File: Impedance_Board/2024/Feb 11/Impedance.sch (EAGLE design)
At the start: 42 parts, among them U2 INA826AID, U4 MC74VHC1GT66DTT1, U7 AD8606ARZ, U8 AD8606ARZ

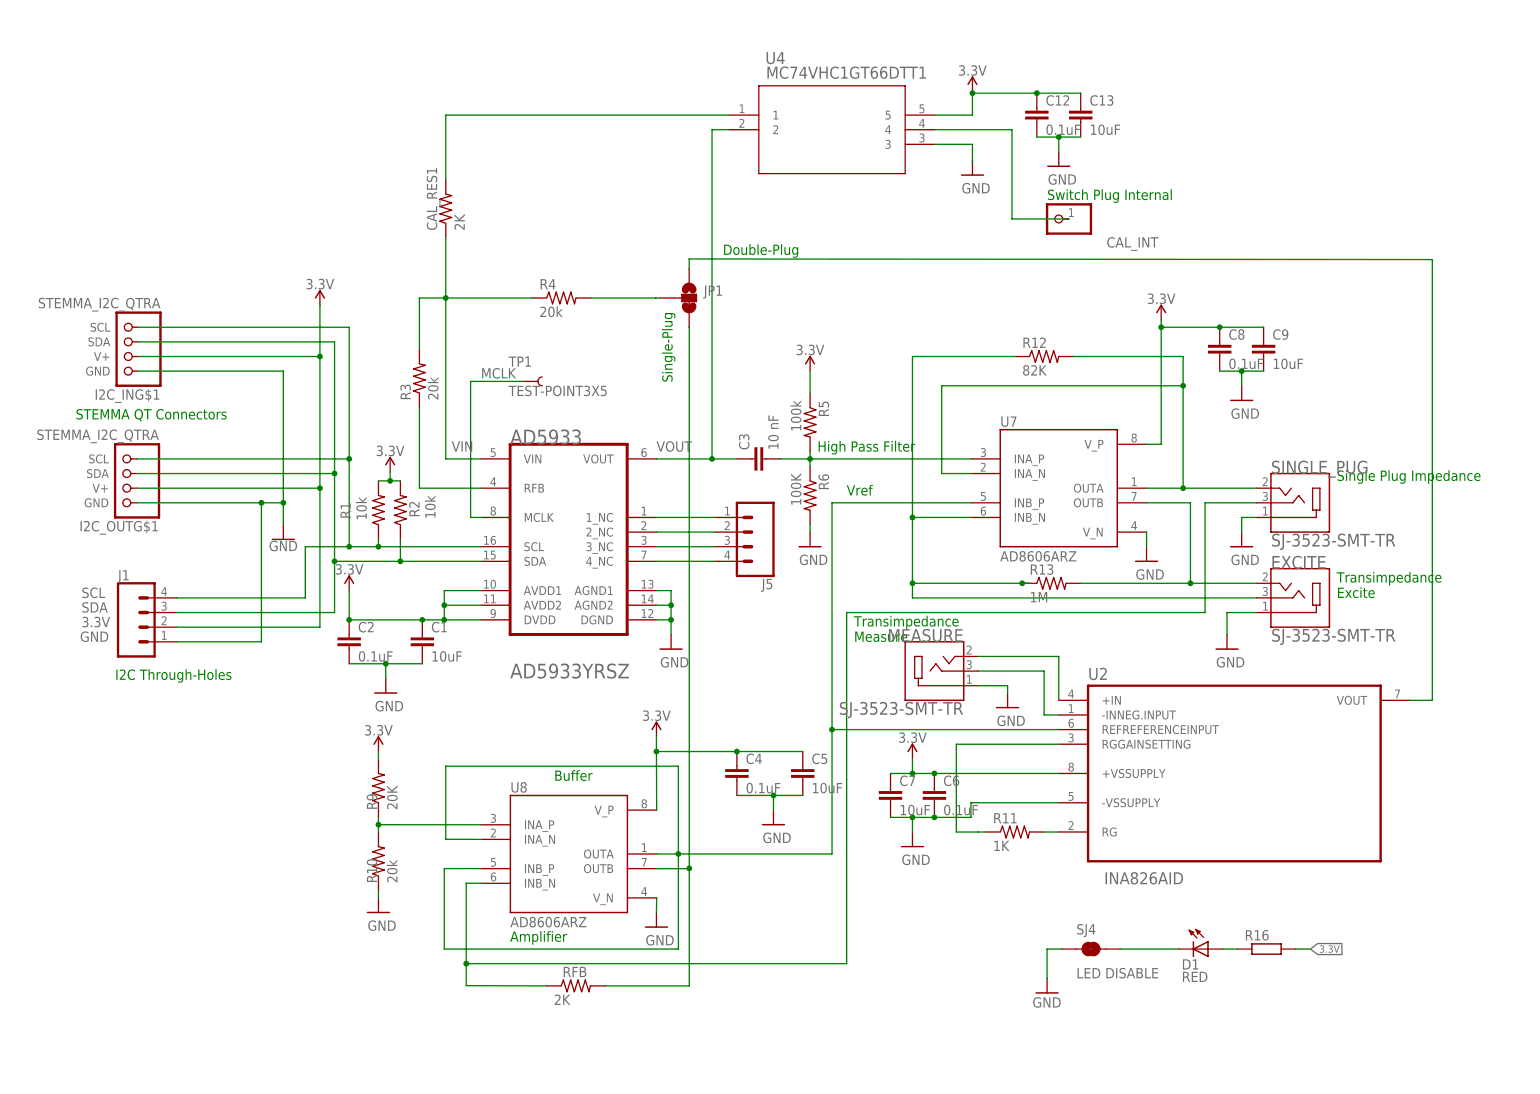
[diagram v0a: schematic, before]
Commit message: Impedance
Minor change SPO2
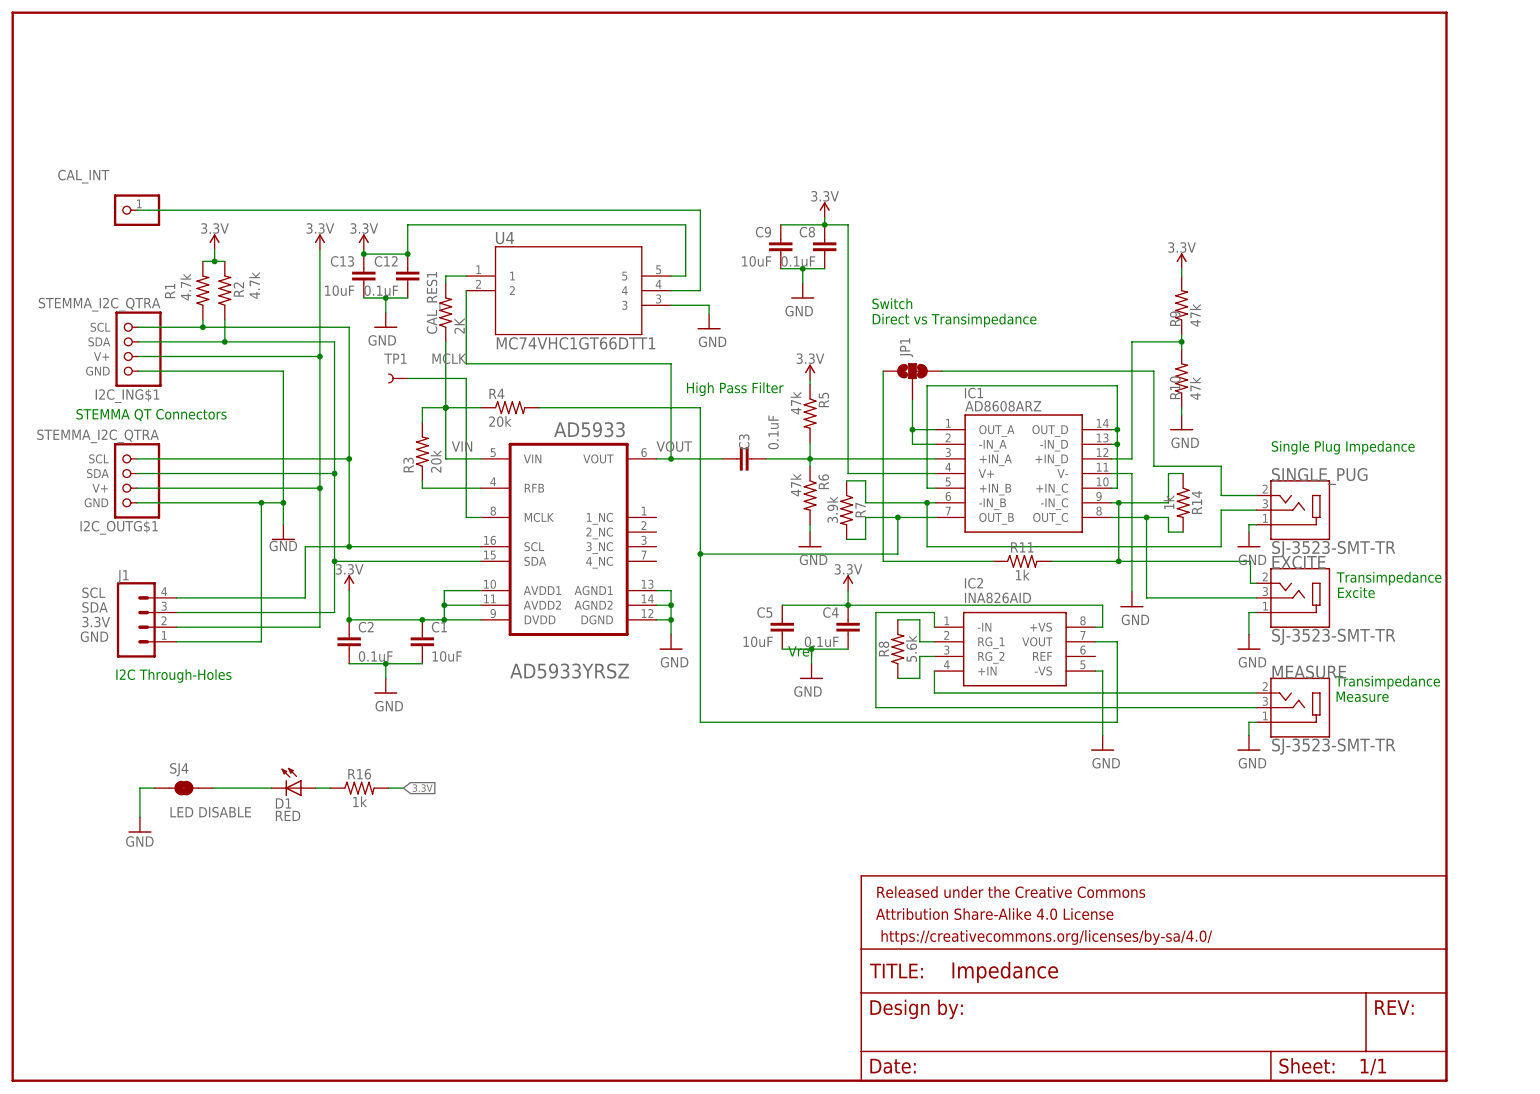
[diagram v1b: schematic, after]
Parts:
- removed C6: 0.1uF, rcl:C-EUC0603
- removed C7: 10uF, rcl:C-EUC0603
- removed J5: (no value), SparkFun-Connectors:CONN_04
- removed R12: 82K, rcl:R-US_R0603
- removed R13: 1M, rcl:R-US_R0603
- removed RFB: 2K, rcl:R-US_R0603
- removed U2: INA826AID, INA826AID:INA826AID
- removed U7, U8: AD8606ARZ, AD8606ARZ:AD8606ARZ
- added FRAME1: FRAME-LETTERNO_PACKAGE, SparkFun-Aesthetics:FRAME-LETTERNO_PACKAGE
- added IC1: AD8608ARZ, AD8608ARZ:AD8608ARZ
- added IC2: INA826AID, INA826AID:INA826AID
- added R14: 1k, SparkFun-Resistors:1KOHM-0603-1/10W-1%
- added R7: 3.9k, SparkFun-Resistors:3.9KOHM-0603-1/10W-1%
- added R8: 5.6k, SparkFun-Resistors:5.6KOHM-0603-1/10W-1%
- C3: value 10 nF -> 0.1uF; device rcl:C-EUC0603 -> SparkFun-Capacitors:0.1UF-0603-25V-(+80/-20%)
- R1, R2: value 10k -> 4.7k; device rcl:R-US_R0603 -> SparkFun-Resistors:4.7KOHM-0603-1/10W-1%
- R10: value 20k -> 47k; device rcl:R-US_R0603 -> SparkFun-Resistors:47KOHM-0603-1/10W-1%
- R11: value 1K -> 1k; device rcl:R-US_R0603 -> SparkFun-Resistors:1KOHM-0603-1/10W-1%
- R16: value R__0603 -> 1k; device JLC PCB Basic Parts_loc:R_1K_0603 -> SparkFun-Resistors:1KOHM-0603-1/10W-1%
- R3, R4: device rcl:R-US_R0603 -> SparkFun-Resistors:20KOHM-0603-1/10W-1%
- R5: value 100k -> 47k; device rcl:R-US_R0603 -> SparkFun-Resistors:47KOHM-0603-1/10W-1%
- R6: value 100K -> 47k; device rcl:R-US_R0603 -> SparkFun-Resistors:47KOHM-0603-1/10W-1%
- R9: value 20K -> 47k; device rcl:R-US_R0603 -> SparkFun-Resistors:47KOHM-0603-1/10W-1%
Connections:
- removed net N$10: AD5933.3_NC, J5.3
- removed net N$11: AD5933.4_NC, J5.4
- removed net N$16: R11.1, U2.RGGAINSETTING
- removed net N$17: RFB.1, SINGLE_PUG.3, U8.INB_N
- removed net N$3: AD5933.1_NC, J5.1
- removed net N$4: AD5933.2_NC, J5.2
- removed net N$7: RFB.2, U8.OUTB
- new net N$22: IC2.RG_1, R8.2
- new net N$6: C3.2, IC1.+IN_A, R5.2, R6.1
- net 3.3V: now also IC1.V+, IC2.+VS; no longer C6.1, C7.1, U2.+VSSUPPLY, U7.V_P, U8.V_P
- net GND: now also IC1.V-, IC2.-VS; no longer C6.2, C7.2, U2.-VSSUPPLY, U7.V_N, U8.V_N
- net N$1: now also IC1.-IN_B, R7.1, SINGLE_PUG.3; no longer JP1.2, R4.2
- net N$13: now also IC1.OUT_B, IC2.VOUT, R4.2, R7.2; no longer U2.REFREFERENCEINPUT, U7.INB_P, U8.INA_N, U8.INB_P, U8.OUTA
- net N$14: now also IC1.+IN_D; no longer U8.INA_P
- net N$15: now also JP1.3; no longer R12.2, U7.INA_N, U7.OUTA
- net N$18: now also IC1.+IN_B, IC1.+IN_C, IC1.-IN_D, IC1.OUT_D; no longer R11.2, U2.RG
- net N$19: now also IC1.-IN_C, R11.2, R14.1; no longer R13.2, U7.OUTB
- net N$20: now also IC2.+IN; no longer U2.+IN
- net N$21: now also IC2.-IN; no longer U2.-INNEG.INPUT
- net N$23: now also IC2.RG_2, R8.1; no longer EXCITE.3, R12.1, R13.1, U7.INB_N
- net N$25: now also EXCITE.3, IC1.OUT_C, R14.2; no longer JP1.1, U2.VOUT
- net N$8: now also JP1.1, R11.1; no longer JP1.3
- net N$9: now also IC1.-IN_A, IC1.OUT_A, JP1.2; no longer C3.2, R5.2, R6.1, U7.INA_P
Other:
- note added: "Switch Direct vs Transimpedance"
- note removed: "Amplifier"
- note removed: "Buffer"
- note removed: "Double-Plug"
- note removed: "Single-Plug"
- note removed: "Switch Plug Internal"
- moved on the sheet: C12, C13, C3, C4, C5, C8, C9, CAL_INT, CAL_RES1, D1, JP1, MEASURE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

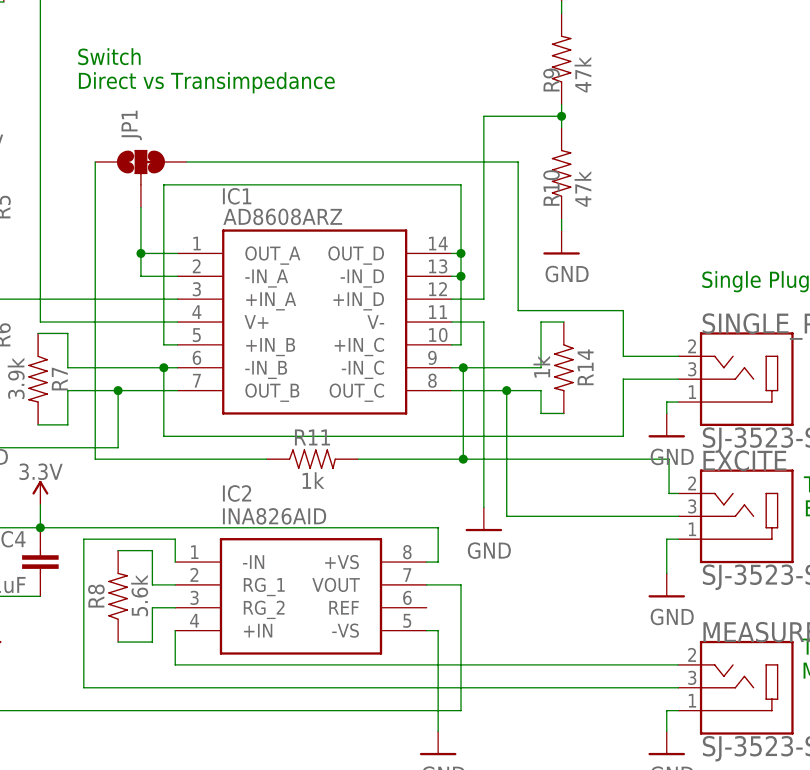
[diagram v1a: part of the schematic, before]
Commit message: Impedance Vref fic
INA needs Vref
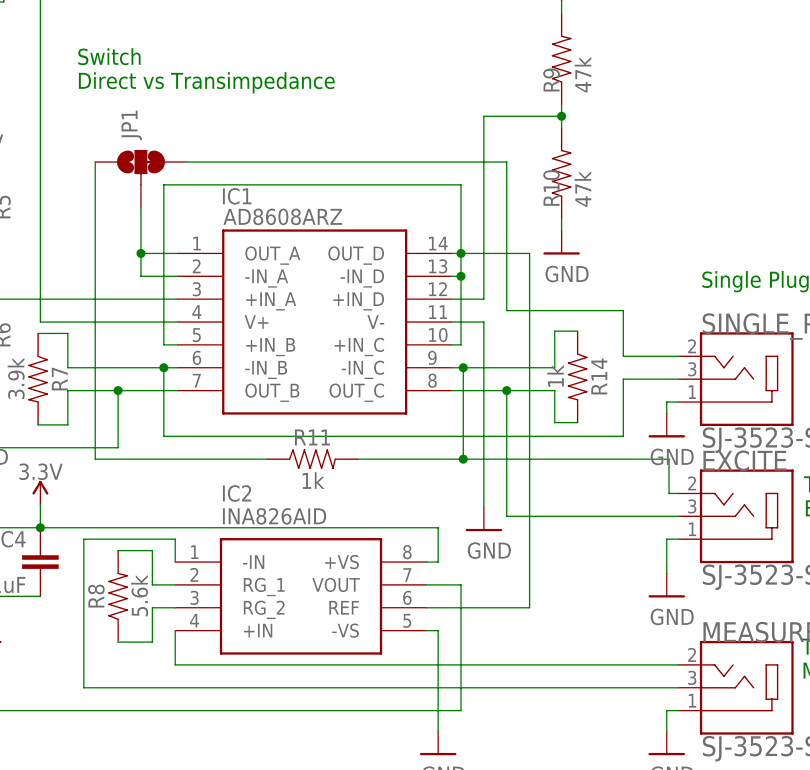
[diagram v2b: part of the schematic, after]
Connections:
- net N$18: now also IC2.REF
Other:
- moved on the sheet: R14
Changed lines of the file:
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@@
 <attribute name="VALUE" x="50.8" y="-10.414" size="1.778" layer="96" font="vector" align="top-center"/>
 </instance>
-<instance part="R14" gate="G$1" x="78.74" y="1.27" smashed="yes" rot="R270">
-<attribute name="NAME" x="80.264" y="1.27" size="1.778" layer="95" font="vector" rot="R270" align="bottom-center"/>
-<attribute name="VALUE" x="77.216" y="1.27" size="1.778" layer="96" font="vector" rot="R270" align="top-center"/>
+<instance part="R14" gate="G$1" x="80.264" y="0.254" smashed="yes" rot="R270">
+<attribute name="NAME" x="81.788" y="0.254" size="1.778" layer="95" font="vector" rot="R270" align="bottom-center"/>
+<attribute name="VALUE" x="78.74" y="0.254" size="1.778" layer="96" font="vector" rot="R270" align="top-center"/>
 </instance>
 <instance part="SUPPLY6" gate="1" x="64.77" y="-41.656" smashed="yes">
@@
 <wire x1="91.44" y1="2.54" x2="85.344" y2="2.54" width="0.1524" layer="91"/>
 <wire x1="85.344" y1="2.54" x2="85.344" y2="7.62" width="0.1524" layer="91"/>
-<wire x1="85.344" y1="7.62" x2="73.66" y2="7.62" width="0.1524" layer="91"/>
+<wire x1="85.344" y1="7.62" x2="72.39" y2="7.62" width="0.1524" layer="91"/>
 <pinref part="JP1" gate="G$1" pin="3"/>
-<wire x1="36.83" y1="24.13" x2="73.66" y2="24.13" width="0.1524" layer="91"/>
-<wire x1="73.66" y1="24.13" x2="73.66" y2="7.62" width="0.1524" layer="91"/>
+<wire x1="36.83" y1="24.13" x2="72.39" y2="24.13" width="0.1524" layer="91"/>
+<wire x1="72.39" y1="24.13" x2="72.39" y2="7.62" width="0.1524" layer="91"/>
 </segment>
 </net>
@@
 <wire x1="67.31" y1="21.59" x2="67.31" y2="13.97" width="0.1524" layer="91"/>
 <junction x="67.31" y="13.97"/>
+<pinref part="IC2" gate="G$1" pin="REF"/>
+<wire x1="63.5" y1="-25.4" x2="74.93" y2="-25.4" width="0.1524" layer="91"/>
+<wire x1="74.93" y1="-25.4" x2="74.93" y2="13.97" width="0.1524" layer="91"/>
+<wire x1="74.93" y1="13.97" x2="67.31" y2="13.97" width="0.1524" layer="91"/>
 </segment>
 </net>
@@
 <segment>
 <pinref part="R14" gate="G$1" pin="2"/>
-<wire x1="78.74" y1="-3.81" x2="76.2" y2="-3.81" width="0.1524" layer="91"/>
+<wire x1="80.264" y1="-4.826" x2="77.724" y2="-4.826" width="0.1524" layer="91"/>
 <pinref part="IC1" gate="G$1" pin="OUT_C"/>
-<wire x1="76.2" y1="-3.81" x2="76.2" y2="-1.27" width="0.1524" layer="91"/>
-<wire x1="76.2" y1="-1.27" x2="72.39" y2="-1.27" width="0.1524" layer="91"/>
+<wire x1="77.724" y1="-4.826" x2="77.724" y2="-1.27" width="0.1524" layer="91"/>
+<wire x1="77.724" y1="-1.27" x2="72.39" y2="-1.27" width="0.1524" layer="91"/>
 <wire x1="72.39" y1="-1.27" x2="66.294" y2="-1.27" width="0.1524" layer="91"/>
 <wire x1="72.39" y1="-15.24" x2="72.39" y2="-1.27" width="0.1524" layer="91"/>
@@
 <wire x1="55.88" y1="-8.89" x2="67.564" y2="-8.89" width="0.1524" layer="91"/>
 <pinref part="R14" gate="G$1" pin="1"/>
-<wire x1="78.74" y1="6.35" x2="76.2" y2="6.35" width="0.1524" layer="91"/>
-<wire x1="67.564" y1="1.27" x2="76.2" y2="1.27" width="0.1524" layer="91"/>
-<wire x1="76.2" y1="1.27" x2="76.2" y2="6.35" width="0.1524" layer="91"/>
+<wire x1="80.264" y1="5.334" x2="77.724" y2="5.334" width="0.1524" layer="91"/>
+<wire x1="67.564" y1="1.27" x2="77.724" y2="1.27" width="0.1524" layer="91"/>
+<wire x1="77.724" y1="1.27" x2="77.724" y2="5.334" width="0.1524" layer="91"/>
 <junction x="67.564" y="1.27"/>
 <wire x1="90.424" y1="-8.89" x2="67.564" y2="-8.89" width="0.1524" layer="91"/>
